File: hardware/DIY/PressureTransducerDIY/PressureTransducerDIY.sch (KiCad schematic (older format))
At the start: 11 parts, among them J1 JST_Power_Connector_Female, J2 PinHeader_Female_MS5803, U1 ATmega328P-PU, U2 MCP1700-3302E_TO92

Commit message: schematic changes
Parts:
- C2: footprint Capacitor_THT:C_Disc_D4.3mm_W1.9mm_P5.00mm -> Capacitor_THT:C_Disc_D3.0mm_W1.6mm_P2.50mm
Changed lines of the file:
@@
 F 0 "C2" H 5665 4446 50  0000 L CNN
 F 1 "1uF" H 5665 4355 50  0000 L CNN
-F 2 "Capacitor_THT:C_Disc_D4.3mm_W1.9mm_P5.00mm" H 5588 4250 50  0001 C CNN
+F 2 "Capacitor_THT:C_Disc_D3.0mm_W1.6mm_P2.50mm" H 5588 4250 50  0001 C CNN
 F 3 "~" H 5550 4400 50  0001 C CNN
 	1    5550 4400

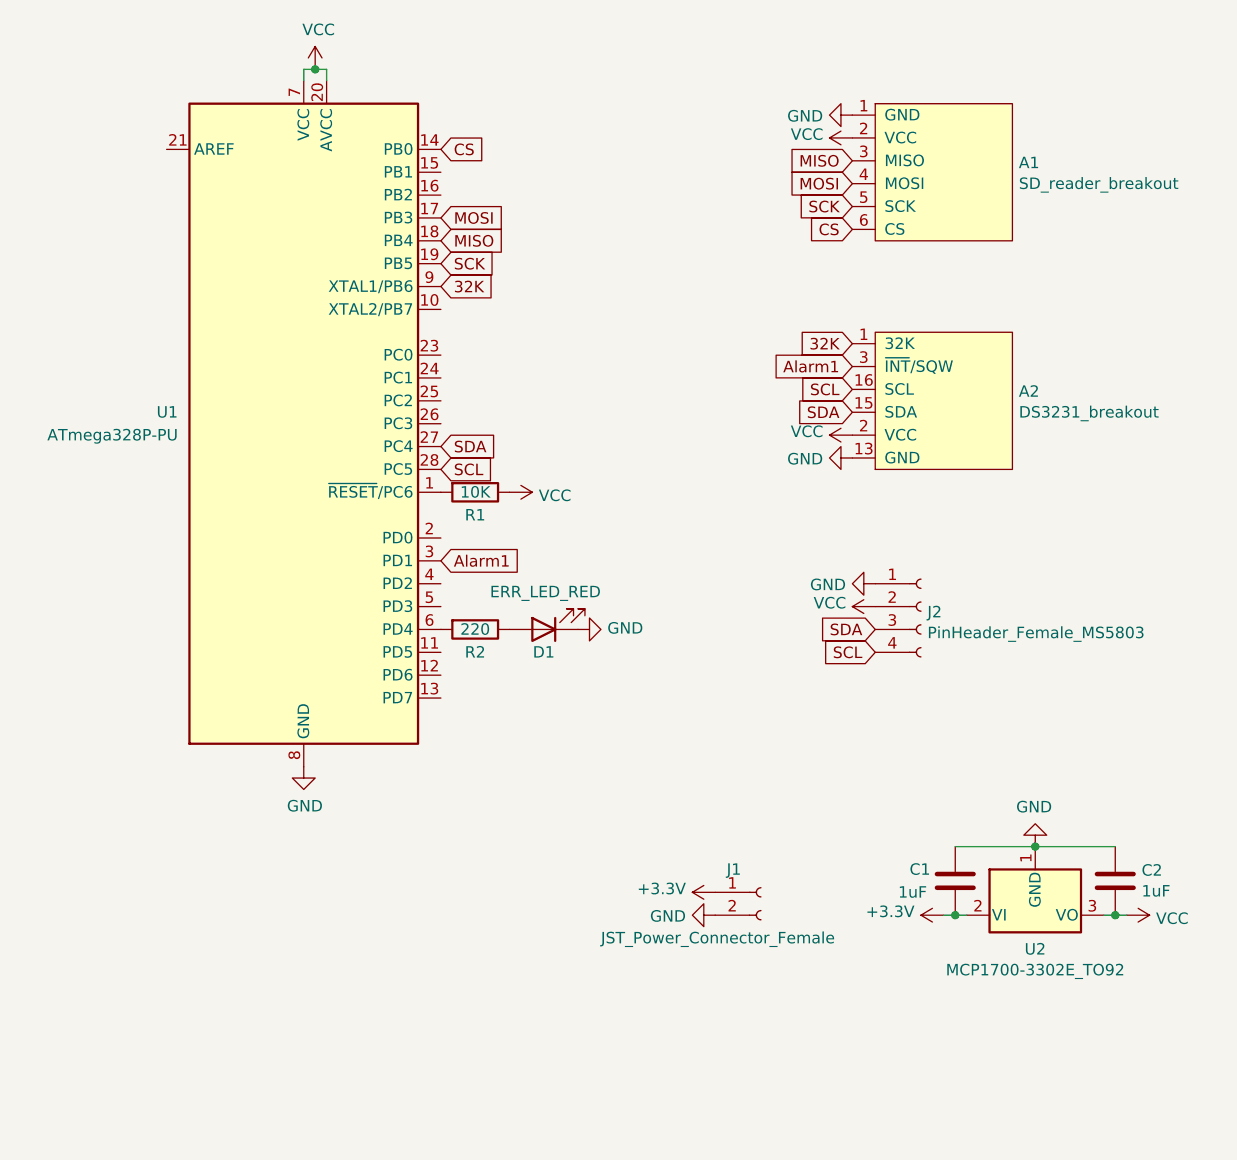
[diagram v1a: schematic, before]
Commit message: Add serial pin header and swap sensor header to JST type
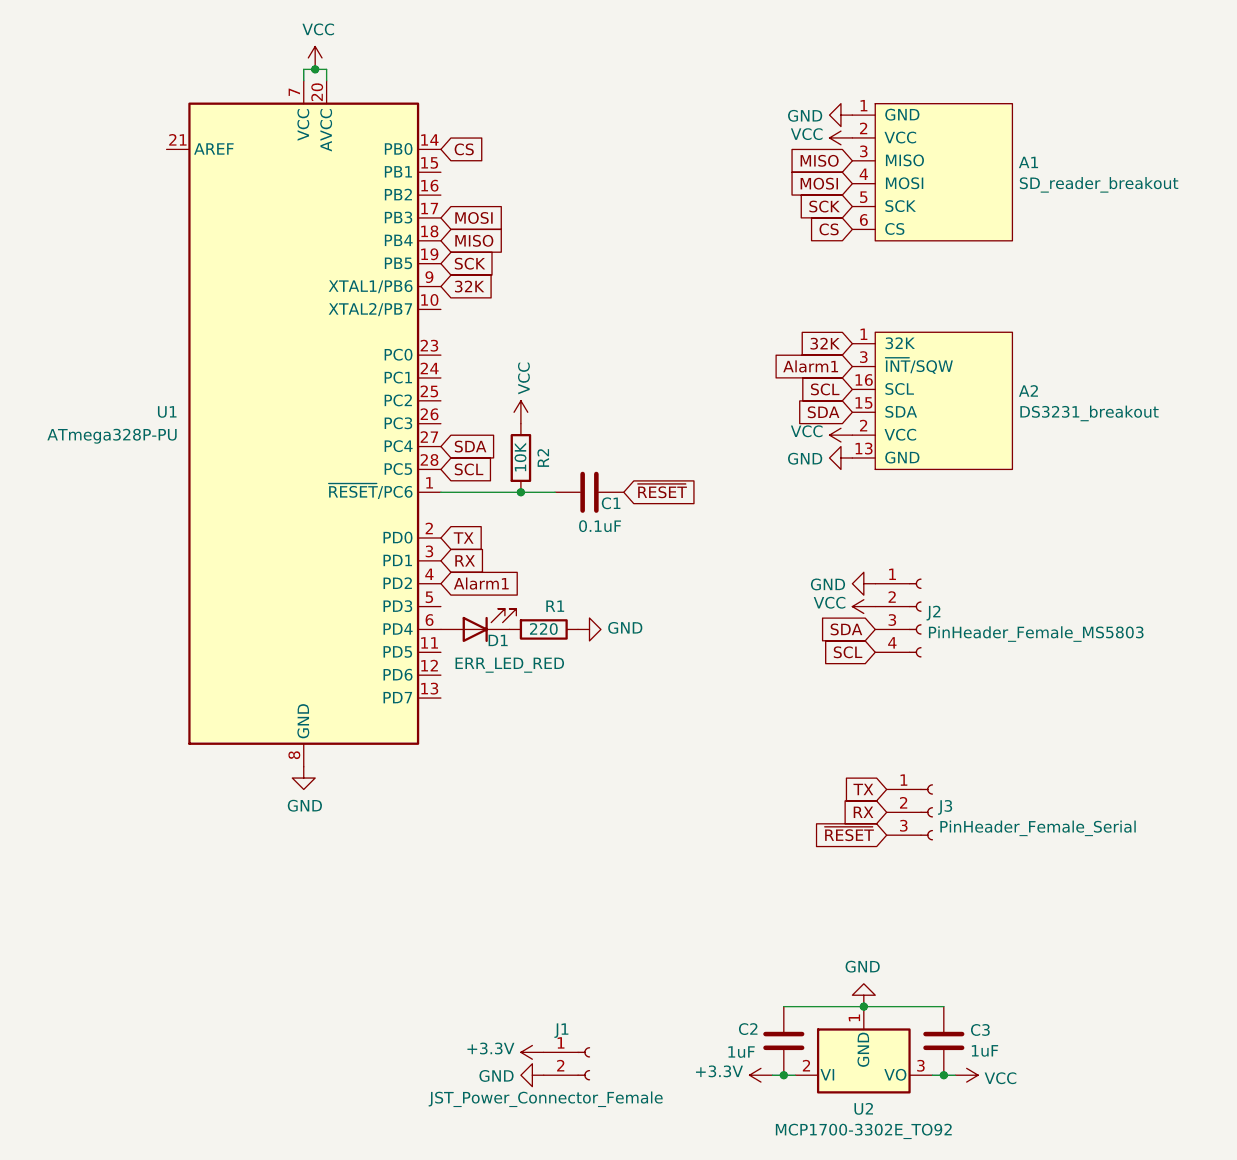
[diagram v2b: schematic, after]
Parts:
- added C1: 0.1uF, Capacitor_THT:C_Disc_D4.3mm_W1.9mm_P5.00mm, symbol Device:C
- added J3: PinHeader_Female_Serial, Connector_PinSocket_2.54mm:PinSocket_1x03_P2.54mm_Vertical, symbol Connector:Conn_01x03_Female
- J2: footprint Connector_PinHeader_2.54mm:PinHeader_1x04_P2.54mm_Vertical -> Connector_JST:JST_EH_S4B-EH_1x04_P2.50mm_Horizontal
- renumbered C1 to C2, C2 to C3, R2 to R1, R1 to R2
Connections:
- net Alarm1: now also U1.4 (PD2); no longer U1.3 (PD1)
- net GND: now also R1.1; no longer D1.1 (K)
- net at R2.2, U1.1 (~RESET~/PC6): now also C1.2
- net TX: now reaches U1.2 (PD0)
- net TX: now also J3.1 (Pin_1)
- net at U1.6 (PD4): now also D1.2 (A); no longer R1.2
- new net: D1.1 (K), R1.2
- new net RX: J3.2 (Pin_2), U1.3 (PD1)
- new net ~RESET: C1.1, J3.3 (Pin_3)
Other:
- moved on the sheet: C2, C3, D1, J1, R1, R2, U2

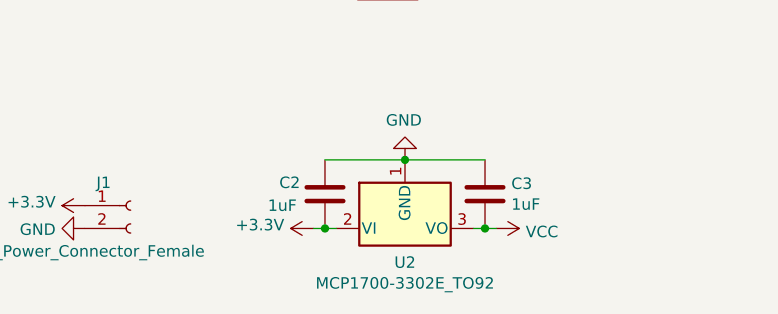
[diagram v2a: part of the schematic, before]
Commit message: Change 4 pin JST to female header, add 3 female pins for Serial programmign
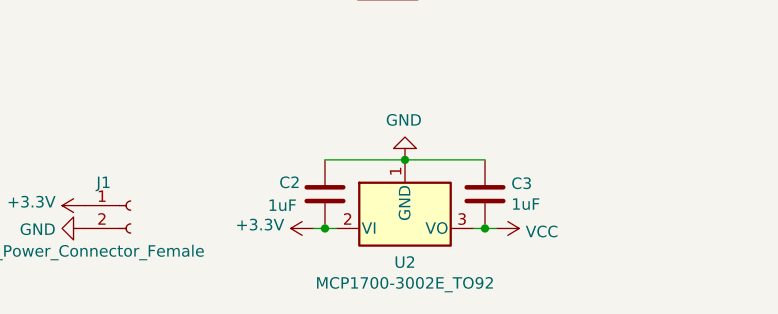
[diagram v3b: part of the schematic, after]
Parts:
- removed U2: MCP1700-3302E_TO92, Package_TO_SOT_THT:TO-92_Inline, symbol Regulator_Linear:MCP1700-3302E_TO92
- added U2: MCP1700-3002E_TO92, Package_TO_SOT_THT:TO-92_Inline_Wide, symbol Regulator_Linear:MCP1700-3002E_TO92
- J2: footprint Connector_JST:JST_EH_S4B-EH_1x04_P2.50mm_Horizontal -> Connector_PinSocket_2.54mm:PinSocket_1x04_P2.54mm_Vertical
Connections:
- net +3V3: now also U2.2 (VI)
- net GND: now also U2.1 (GND)
- net VCC: now also U2.3 (VO)
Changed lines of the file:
@@
-$EndComp
-$Comp
-L Regulator_Linear:MCP1700-3302E_TO92 U2
-U 1 1 60A696A2
-P 4450 5250
-F 0 "U2" H 4450 5101 50  0000 C CNN
-F 1 "MCP1700-3302E_TO92" H 4450 5010 50  0000 C CNN
-F 2 "Package_TO_SOT_THT:TO-92_Inline" H 4450 5050 50  0001 C CIN
-F 3 "http://ww1.microchip.com/downloads/en/DeviceDoc/20001826D.pdf" H 4450 5250 50  0001 C CNN
-	1    4450 5250
-	1    0    0    -1
 $EndComp
 $Comp
@@
 F 0 "J2" H 4728 3176 50  0000 L CNN
 F 1 "PinHeader_Female_MS5803" H 4728 3085 50  0000 L CNN
-F 2 "Connector_JST:JST_EH_S4B-EH_1x04_P2.50mm_Horizontal" H 4700 3200 50  0001 C CNN
+F 2 "Connector_PinSocket_2.54mm:PinSocket_1x04_P2.54mm_Vertical" H 4700 3200 50  0001 C CNN
 F 3 "~" H 4700 3200 50  0001 C CNN
 	1    4700 3200
@@
 	0    1    1    0
 $EndComp
+$Comp
+L Regulator_Linear:MCP1700-3002E_TO92 U2
+U 1 1 60D54F28
+P 4450 5250
+F 0 "U2" H 4450 5101 50  0000 C CNN
+F 1 "MCP1700-3002E_TO92" H 4450 5010 50  0000 C CNN
+F 2 "Package_TO_SOT_THT:TO-92_Inline_Wide" H 4450 5050 50  0001 C CIN
+F 3 "http://ww1.microchip.com/downloads/en/DeviceDoc/20001826D.pdf" H 4450 5250 50  0001 C CNN
+	1    4450 5250
+	1    0    0    -1
+$EndComp
 $EndSCHEMATC

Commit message: Restart for new set of assembly photos
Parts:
- A1: symbol Breakouts:SD_reader_breakout -> PressureTransducerDIY-rescue:SD_reader_breakout-Breakouts
- A2: symbol Breakouts:DS3231_breakout -> PressureTransducerDIY-rescue:DS3231_breakout-Breakouts
- J1: footprint Connector_JST:JST_PH_S2B-PH-K_1x02_P2.00mm_Horizontal -> Connector_JST:JST_PH_B2B-PH-K_1x02_P2.00mm_Vertical
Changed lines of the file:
@@
 $EndComp
 $Comp
-L Breakouts:DS3231_breakout A2
+L PressureTransducerDIY-rescue:DS3231_breakout-Breakouts A2
 U 1 1 60A4A9F0
 P 4800 2300
@@
 $EndComp
 $Comp
-L Breakouts:SD_reader_breakout A1
+L PressureTransducerDIY-rescue:SD_reader_breakout-Breakouts A1
 U 1 1 60A4BD05
 P 4800 1300
@@
 F 0 "J1" H 3100 5250 50  0000 L CNN
 F 1 "JST_Power_Connector_Female" H 2550 4950 50  0000 L CNN
-F 2 "Connector_JST:JST_PH_S2B-PH-K_1x02_P2.00mm_Horizontal" H 3250 5150 50  0001 C CNN
+F 2 "Connector_JST:JST_PH_B2B-PH-K_1x02_P2.00mm_Vertical" H 3250 5150 50  0001 C CNN
 F 3 "~" H 3250 5150 50  0001 C CNN
 	1    3250 5150
